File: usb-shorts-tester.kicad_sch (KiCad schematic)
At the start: 4 parts, among them J1 CX60-24S-UNIT, J2 USB4080-03-A_REVA1, U1 TCA6424ARGJR

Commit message: Beta release
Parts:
- added C1: 0.1uF, Capacitor_SMD:C_0603_1608Metric, symbol Device:C_Small
- added JP1: I2C0_I2C1_SDA_JMP_Bridged_12, Jumper:SolderJumper-3_P1.3mm_Bridged12_RoundedPad1.0x1.5mm, symbol Jumper:SolderJumper_3_Bridged12
- added JP2: I2C0_I2C1_SCL_JMP_Bridged_12, Jumper:SolderJumper-3_P1.3mm_Bridged12_RoundedPad1.0x1.5mm, symbol Jumper:SolderJumper_3_Bridged12
- added JP5: JMP_ADDR, Jumper:SolderJumper-2_P1.3mm_Open_RoundedPad1.0x1.5mm, symbol Jumper:SolderJumper_2_Open
- added JP6: I2C_PULLUP_JMP_CLOSED, Jumper:SolderJumper-3_P1.3mm_Bridged12_RoundedPad1.0x1.5mm, symbol Jumper:SolderJumper_3_Bridged123
- added R1, R2: 4k7, Resistor_SMD:R_0603_1608Metric, symbol Device:R_Small
- added R3, R4: 10k, Resistor_SMD:R_0603_1608Metric, symbol Device:R_Small
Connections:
- net +3V3: now also C1.2, JP5.1 (A), JP6.2 (C), R4.1
- net GND: now also C1.1, R3.2
- net ADDR: now reaches U1.26 (ADDR)
- net ADDR: now also JP5.2 (B), R3.1
- net SCL: now reaches U1.29 (SCL)
- net SCL: now also JP2.2 (C), R1.2
- net SDA: now reaches U1.30 (SDA)
- net SDA: now also JP1.2 (C), R2.2
- net at U1.32 (~{INT}): now also R4.2
- net GPIO7: now reaches A1.10 (GPIO7)
- net GPIO7: now also JP2.3 (B)
- net GPIO20: now reaches A1.26 (GPIO20)
- net GPIO20: now also JP1.1 (A)
- net GPIO21: now reaches A1.27 (GPIO21)
- net GPIO21: now also JP2.1 (A)
- net GPIO6: now reaches A1.9 (GPIO6)
- net GPIO6: now also JP1.3 (B)
- new net: JP6.3 (B), R2.1
- new net: JP6.1 (A), R1.1
- no-connect marks 40 -> 36
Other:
- moved on the sheet: U1

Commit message: Add usb shield probing
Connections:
- net SHIELD: now reaches J2.G1 (SHIELD), J2.G2 (SHIELD), J2.G3 (SHIELD), J2.G4 (SHIELD)
- net SHIELD: now also A1.29 (GPIO22), J1.S1 (SHIELD1), J1.S2 (SHIELD1), J1.S3 (SHIELD2), J1.S4 (SHIELD2)
- no-connect marks 36 -> 34
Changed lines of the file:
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@@
 (kicad_sch (version 20230121) (generator eeschema)
   (paper "A4")
+  (junction (at 62.865 156.845) (diameter 0) (color 0 0 0 0)
+  )
   (junction (at 172.72 76.2) (diameter 0) (color 0 0 0 0)
+  )
+  (junction (at 65.405 156.845) (diameter 0) (color 0 0 0 0)
+  )
+  (junction (at 60.325 156.845) (diameter 0) (color 0 0 0 0)
   )
   (junction (at 259.08 28.575) (diameter 0) (color 0 0 0 0)
@@
   (no_connect (at 48.26 46.355))
   (no_connect (at 48.26 36.195))
-  (no_connect (at 83.82 64.135))
   (no_connect (at 48.26 38.735))
   (no_connect (at 48.26 71.755))
@@
   (no_connect (at 48.26 48.895))
   (no_connect (at 65.405 156.845))
-  (no_connect (at 127.635 148.59))
   (no_connect (at 68.58 89.535))
   (no_connect (at 83.82 51.435))
@@
   (no_connect (at 83.82 53.975))
   (no_connect (at 83.82 56.515))
+  (wire (pts (xy 62.865 156.845) (xy 65.405 156.845))
+    (stroke (width 0) (type default))
+  )
   (wire (pts (xy 255.27 28.575) (xy 259.08 28.575))
     (stroke (width 0) (type default))
@@
     (stroke (width 0) (type default))
   )
+  (wire (pts (xy 65.405 156.845) (xy 69.85 156.845))
+    (stroke (width 0) (type default))
+  )
   (wire (pts (xy 133.35 97.79) (xy 136.525 97.79))
     (stroke (width 0) (type default))
@@
     (stroke (width 0) (type default))
   )
+  (wire (pts (xy 60.325 156.845) (xy 62.865 156.845))
+    (stroke (width 0) (type default))
+  )
   (wire (pts (xy 252.73 34.29) (xy 252.73 36.83))
     (stroke (width 0) (type default))
   )
+  (wire (pts (xy 57.785 156.845) (xy 60.325 156.845))
+    (stroke (width 0) (type default))
+  )
   (wire (pts (xy 259.08 34.925) (xy 259.08 36.195))
     (stroke (width 0) (type default))
@@
     )
   )
+  (global_label "SHIELD" (shape input) (at 127.635 148.59 180) (fields_autoplaced)
+    (effects (font (size 1.27 1.27)) (justify right))
+    (property "Intersheetrefs" "${INTERSHEET_REFS}" (at 118.1373 148.59 0)
+      (effects (font (size 1.27 1.27)) (justify right) hide)
+    )
+  )
   (global_label "A6" (shape input) (at 217.17 64.77 180) (fields_autoplaced)
     (effects (font (size 1.27 1.27)) (justify right))
@@
     )
   )
+  (global_label "SHIELD" (shape input) (at 83.82 64.135 0) (fields_autoplaced)
+    (effects (font (size 1.27 1.27)) (justify left))
+    (property "Intersheetrefs" "${INTERSHEET_REFS}" (at 93.3177 64.135 0)
+      (effects (font (size 1.27 1.27)) (justify left) hide)
+    )
+  )
   (global_label "GPIO21" (shape input) (at 83.82 69.215 0) (fields_autoplaced)
     (effects (font (size 1.27 1.27)) (justify left))
@@
       (effects (font (size 1.27 1.27)) (justify left) hide)
     )
+  )
+  (global_label "SHIELD" (shape input) (at 69.85 156.845 0) (fields_autoplaced)
+    (effects (font (size 1.27 1.27)) (justify left))
+    (property "Intersheetrefs" "${INTERSHEET_REFS}" (at 79.3477 156.845 0)
+      (effects (font (size 1.27 1.27)) (justify left) hide)
+    )

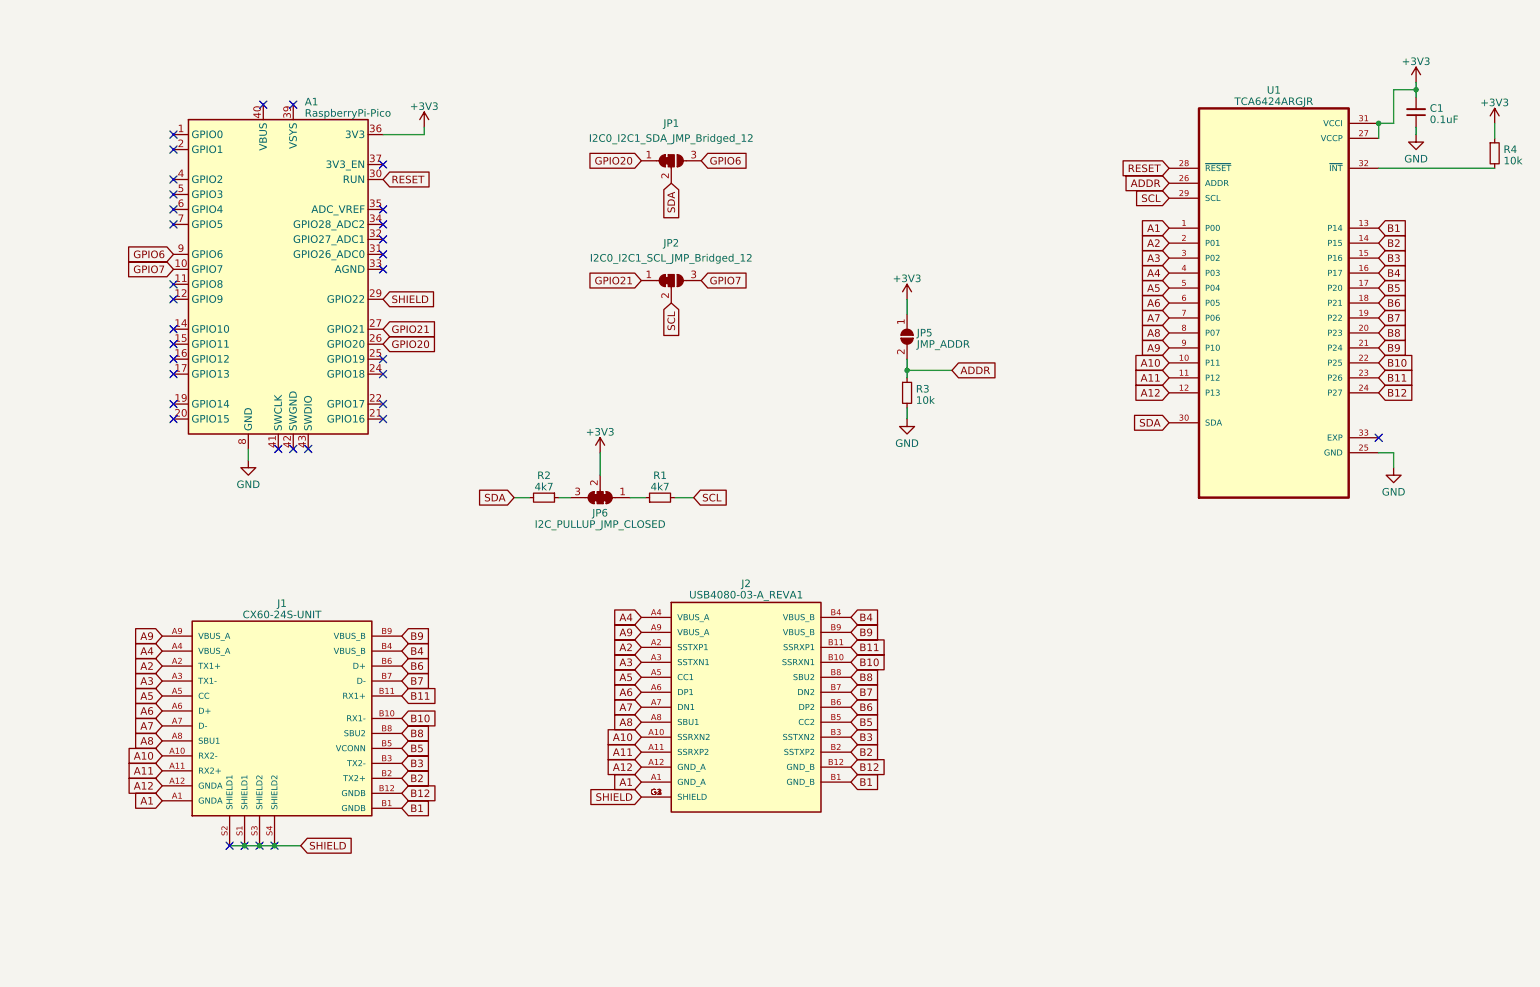
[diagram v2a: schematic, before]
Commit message: Add pulldowns on all expander pins
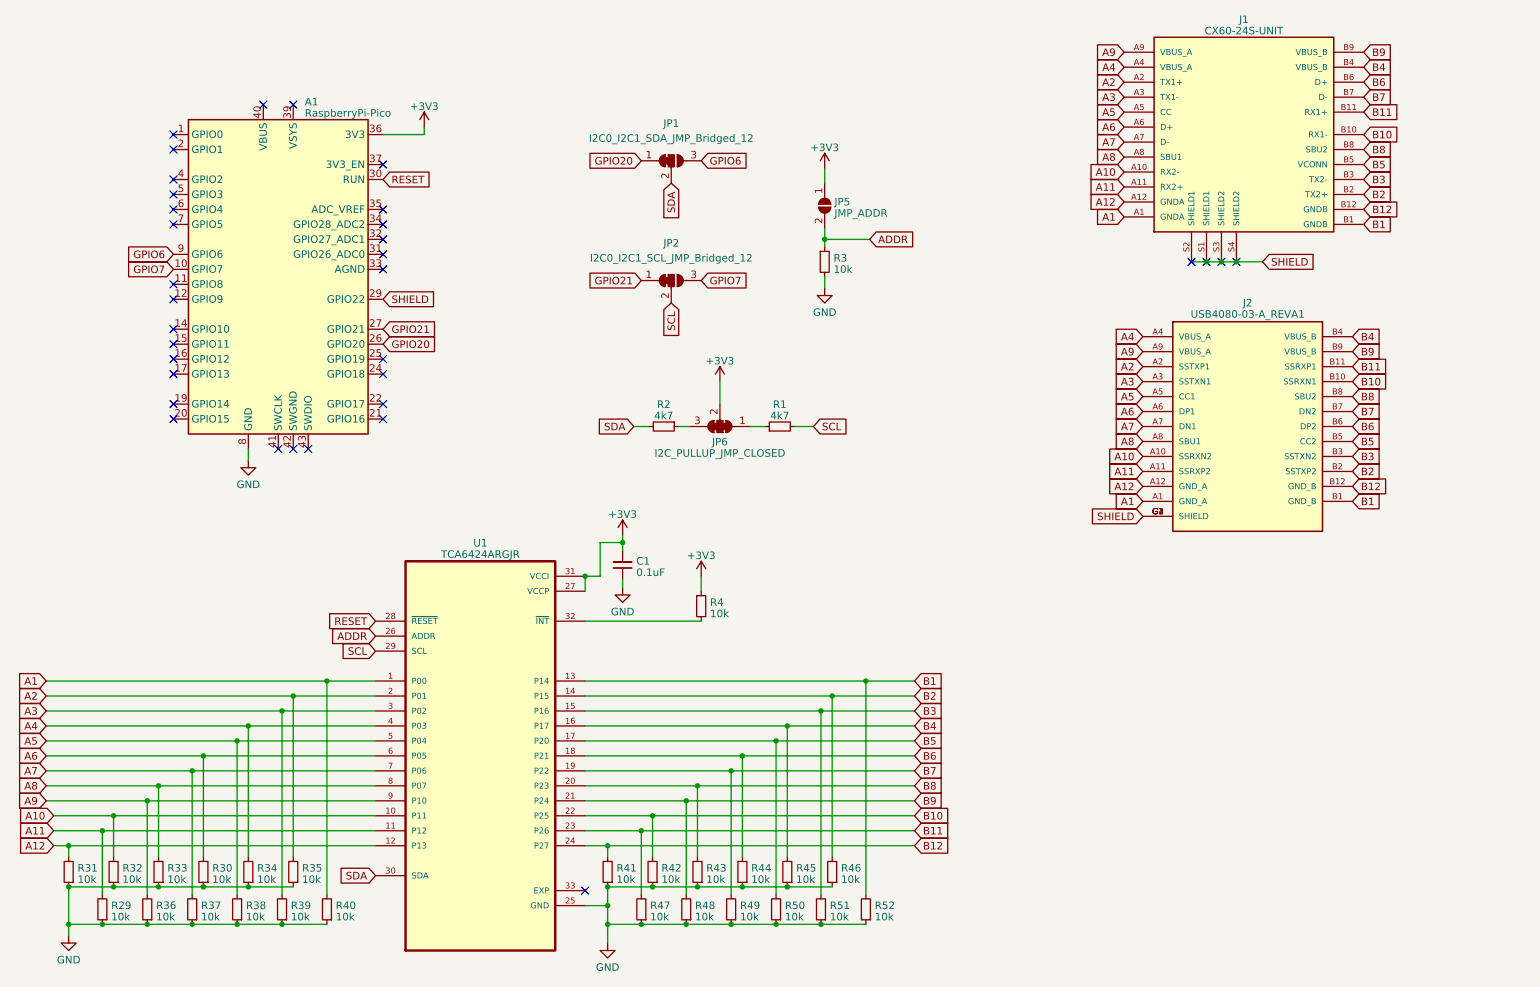
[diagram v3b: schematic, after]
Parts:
- added R29, R30, R31, R32, R33, R34, R35, R36, R37, R38, R39, R40, R41, R42, R43, R44, R45, R46, R47, R48, R49, R50, R51, R52: 10k, Resistor_SMD:R_0603_1608Metric, symbol Device:R_Small
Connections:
- net A1: now also R40.2
- net A10: now also R32.2
- net A11: now also R29.2
- net A12: now also R31.2
- net A2: now also R35.2
- net A3: now also R39.2
- net A4: now also R34.2
- net A5: now also R38.2
- net A6: now also R30.2
- net A7: now also R37.2
- net A8: now also R33.2
- net A9: now also R36.2
- net B1: now also R52.2
- net B10: now also R42.2
- net B11: now also R47.2
- net B12: now also R41.2
- net B2: now also R46.2
- net B3: now also R51.2
- net B4: now also R45.2
- net B5: now also R50.2
- net B6: now also R44.2
- net B7: now also R49.2
- net B8: now also R43.2
- net B9: now also R48.2
- net GND: now also R29.1, R30.1, R31.1, R32.1, R33.1, R34.1, R35.1, R36.1, R37.1, R38.1, R39.1, R40.1, R41.1, R42.1, R43.1, R44.1, R45.1, R46.1, R47.1, R48.1, R49.1, R50.1, R51.1, R52.1
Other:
- moved on the sheet: C1, J1, J2, JP5, JP6, R1, R2, R3, R4, U1
